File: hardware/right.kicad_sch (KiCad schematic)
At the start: 0 parts

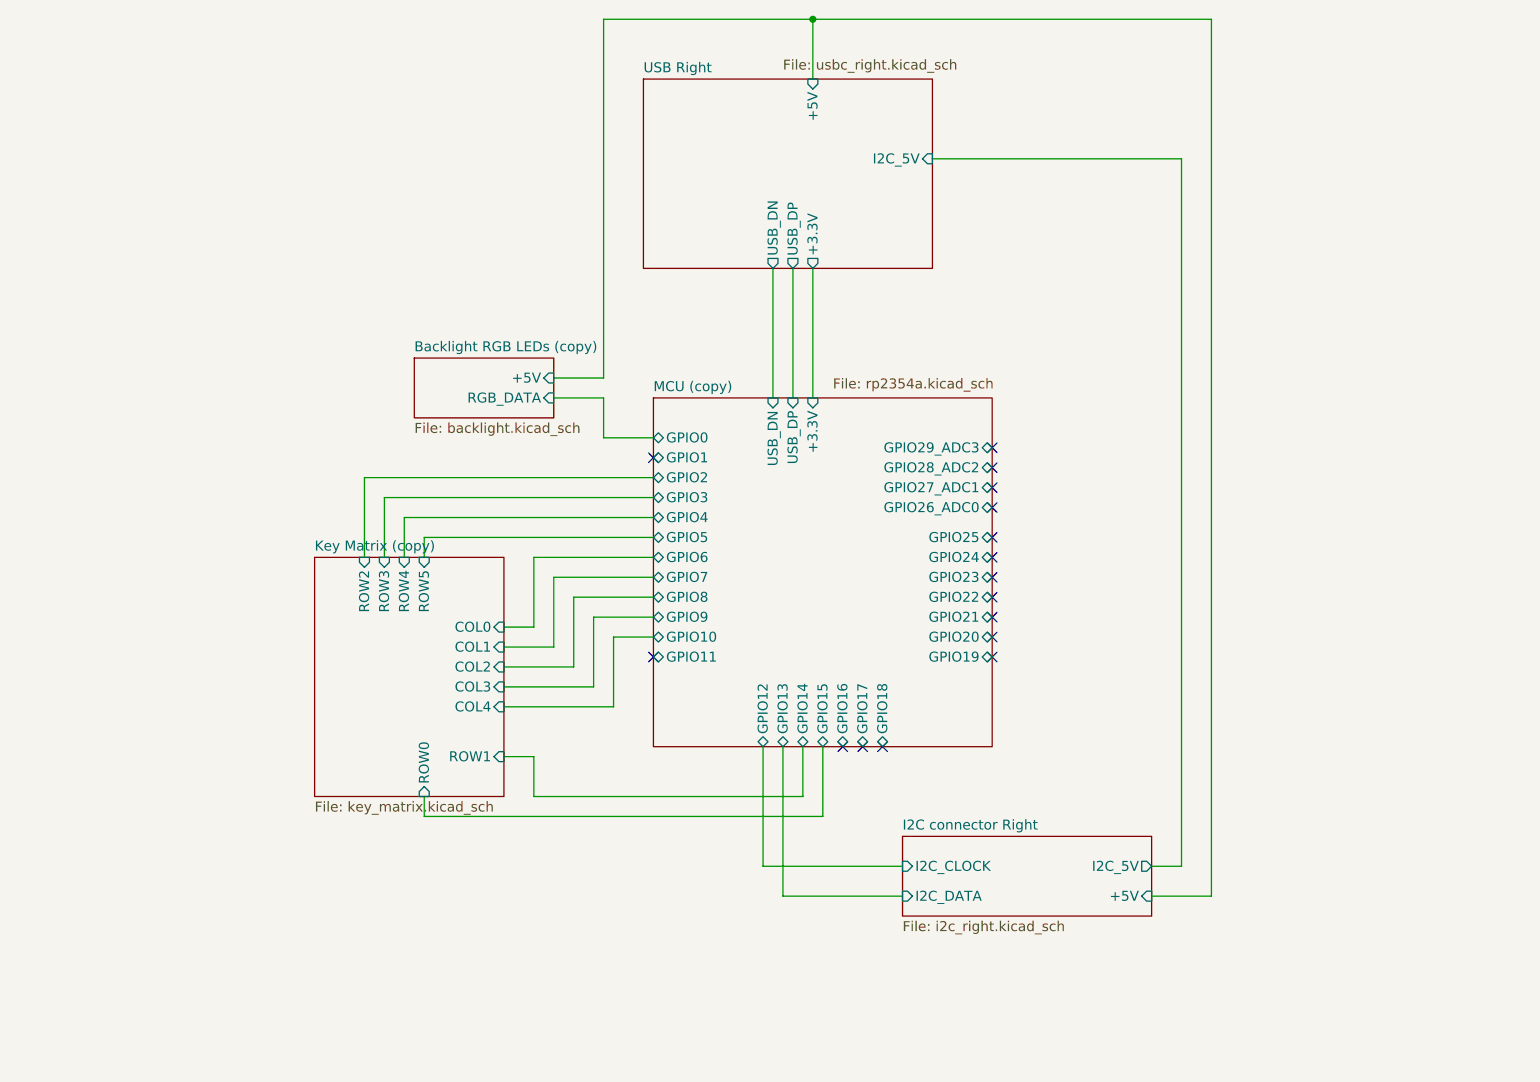
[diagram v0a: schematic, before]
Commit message: encoder to schematic
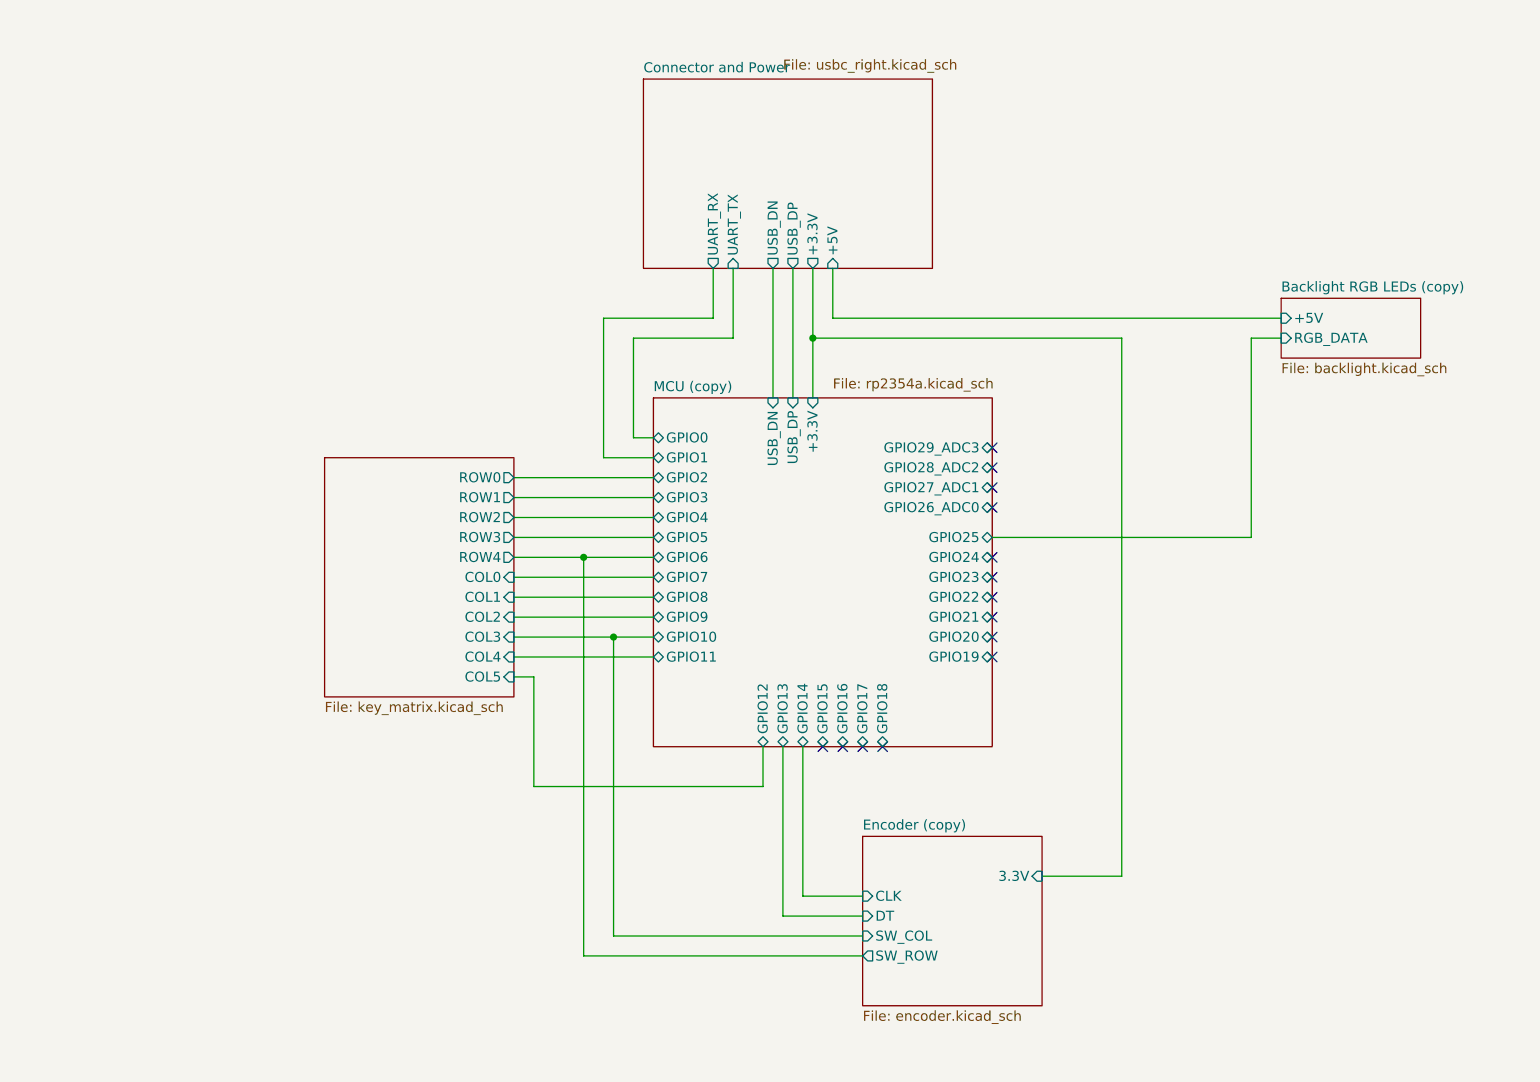
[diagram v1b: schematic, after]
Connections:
- no-connect marks 16 -> 14
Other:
- sheet USB Right renamed Connector and Power
- removed sheet I2C connector Right
- added sheet Encoder (copy) (encoder.kicad_sch)
- sheet Connector and Power ports: added UART_RX, UART_TX; removed I2C_5V
- sheet Key Matrix (copy) ports: added COL5; removed ROW5

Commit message: electronics
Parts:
- added PCB shape left2: (no value), rp_voyager:PCB left, symbol rp_voyager:PCB_left
- added Realestateleft2: (no value), rp_voyager:Realestate left, symbol rp_voyager:realestate_left
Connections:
- no-connect marks 14 -> 12
